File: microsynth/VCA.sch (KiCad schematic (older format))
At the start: 33 parts, among them J1 AudioJack3, J8 AudioJack2, Q9 BC548, U21 CA3080, U23 LM380N

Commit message: Replace dodgy parts 1458, 4136 & LF351s
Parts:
- U23: footprint Package_DIP:DIP-14_W7.62mm -> Package_DIP:DIP-14_W7.62mm_LongPads
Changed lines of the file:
@@
 F 0 "U23" H 7300 1700 50  0000 L CNN
 F 1 "LM380N" H 7400 1550 50  0000 L CNN
-F 2 "Package_DIP:DIP-14_W7.62mm" H 7350 1700 50  0001 C CIN
+F 2 "Package_DIP:DIP-14_W7.62mm_LongPads" H 7350 1700 50  0001 C CIN
 F 3 "http://www.ti.com/lit/ds/symlink/lm380.pdf" H 7350 1700 50  0001 C CNN
 	1    7350 1700

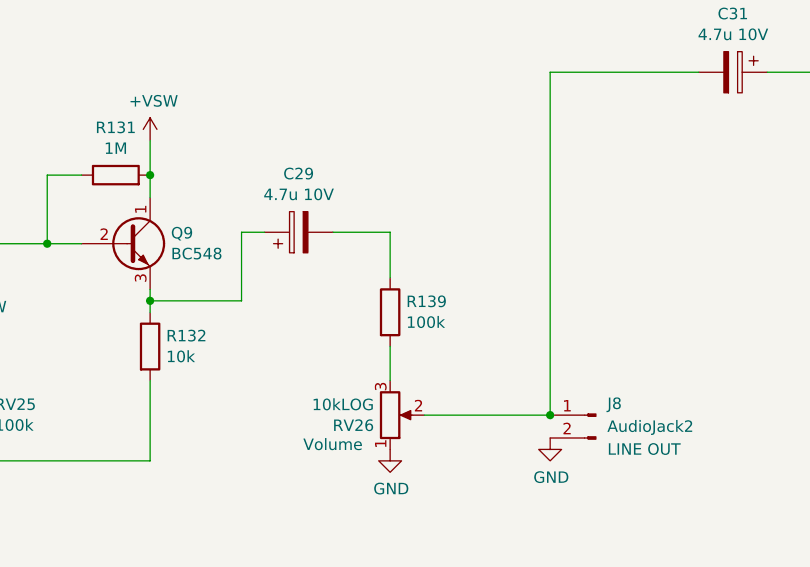
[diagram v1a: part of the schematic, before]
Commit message: Add test points
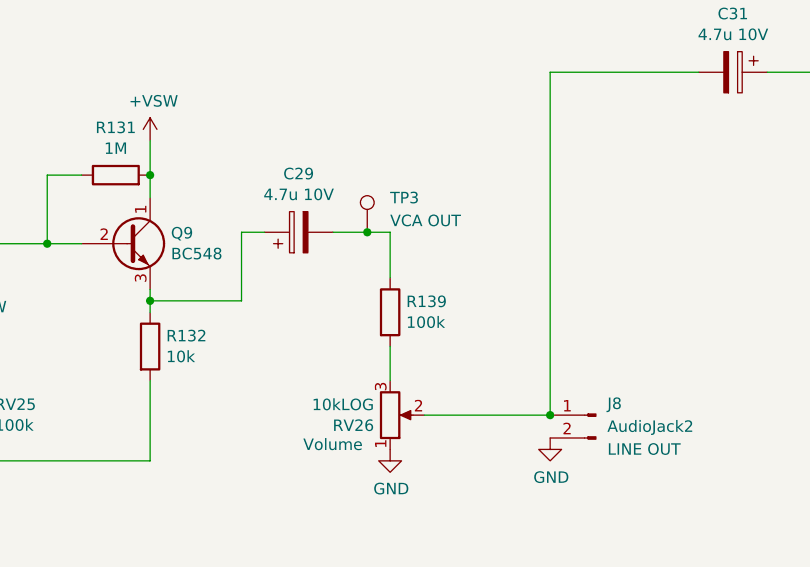
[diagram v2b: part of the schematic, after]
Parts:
- added TP3: VCA OUT, TestPoint:TestPoint_Pad_D2.0mm, symbol Connector:TestPoint
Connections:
- net at C29.2, R139.1: now also TP3.1
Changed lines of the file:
@@
 	3950 2800 3950 2750
 Wire Wire Line
-	4750 2500 5000 2500
+	4750 2500 4900 2500
 Wire Wire Line
 	5000 2500 5000 2700
@@
 	1    0    0    1
 $EndComp
-Wire Wire Line
-	5000 3150 5000 3000
 $Comp
 L power:GND #PWR?
@@
 $EndComp
 Connection ~ 5700 3300
+$Comp
+L Connector:TestPoint TP?
+U 1 1 5EE088D7
+P 4900 2500
+AR Path="/5E475532/5EE088D7" Ref="TP?"  Part="1"
+AR Path="/5E1B03E8/5EE088D7" Ref="TP3"  Part="1"
+F 0 "TP3" H 5000 2650 50  0000 L CNN
+F 1 "VCA OUT" H 5000 2550 50  0000 L CNN
+F 2 "TestPoint:TestPoint_Pad_D2.0mm" H 5100 2500 50  0001 C CNN
+F 3 "~" H 5100 2500 50  0001 C CNN
+	1    4900 2500
+	1    0    0    -1
+$EndComp
+Connection ~ 4900 2500
+Wire Wire Line
+	4900 2500 5000 2500
+Wire Wire Line
+	5000 3000 5000 3150
 $EndSCHEMATC

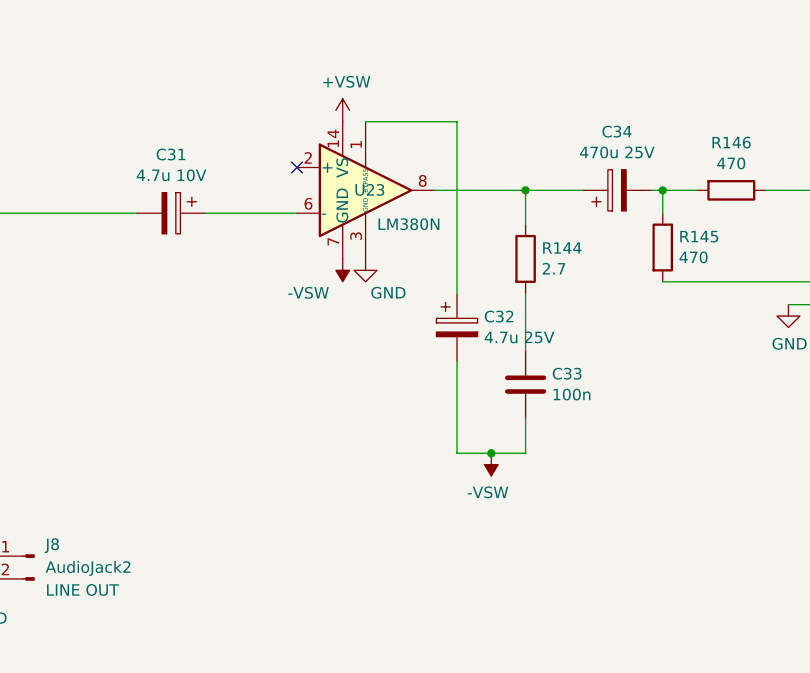
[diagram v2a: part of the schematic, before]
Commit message: Fix output amp
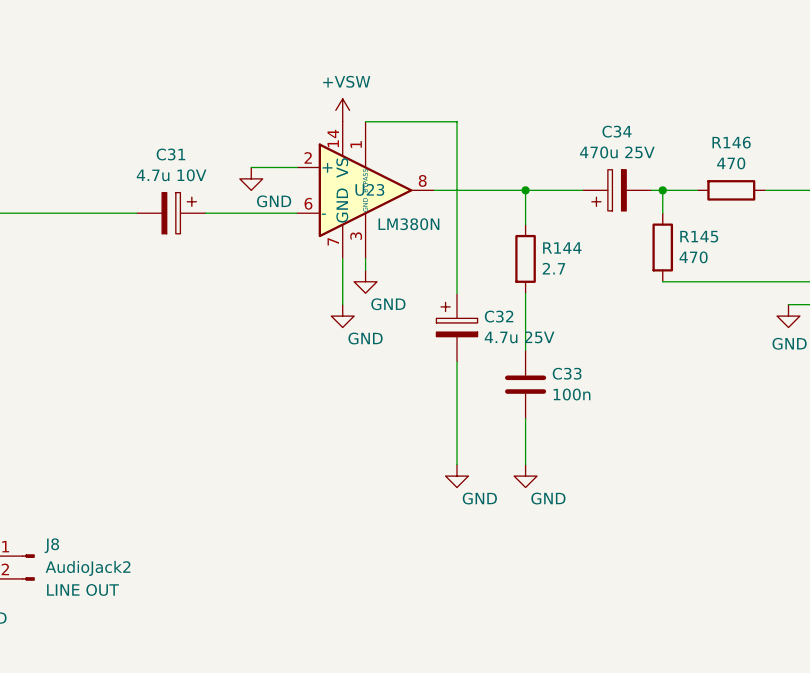
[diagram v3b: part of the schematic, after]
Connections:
- net -VSW: no longer C32.2, C33.2, U23.7 (GND)
- net GND: now also C32.2, C33.2, U23.2 (+), U23.7 (GND)
- no-connect marks 1 -> 0
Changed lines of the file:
@@
 	1    0    0    -1
-$EndComp
-$Comp
-L power:-VSW #PWR?
-U 1 1 5E1EC995
-P 7250 2000
-F 0 "#PWR?" H 7250 2100 50  0001 C CNN
-F 1 "-VSW" H 7400 2150 50  0000 C CNN
-F 2 "" H 7250 2000 50  0001 C CNN
-F 3 "" H 7250 2000 50  0001 C CNN
-	1    7250 2000
-	-1   0    0    1
 $EndComp
 Wire Wire Line
@@
 Wire Wire Line
 	8050 1700 8300 1700
-$Comp
-L power:-VSW #PWR?
-U 1 1 5E1F94DC
-P 7900 2850
-F 0 "#PWR?" H 7900 2950 50  0001 C CNN
-F 1 "-VSW" H 7915 3023 50  0000 C CNN
-F 2 "" H 7900 2850 50  0001 C CNN
-F 3 "" H 7900 2850 50  0001 C CNN
-	1    7900 2850
-	-1   0    0    1
-$EndComp
 Wire Wire Line
 	7050 1800 6650 1800
-NoConn ~ 7050 1600
 $Comp
 L Device:C C33
@@
 Wire Wire Line
 	8050 2400 8050 2150
-Wire Wire Line
-	8050 2700 8050 2850
-Wire Wire Line
-	8050 2850 7900 2850
-Wire Wire Line
-	7750 2450 7750 2850
-Connection ~ 7900 2850
-Wire Wire Line
-	7900 2850 7750 2850
 Text GLabel 1050 3450 0    50   BiDi ~ 0
 VCF_OUT
@@
 L power:GND #PWR?
 U 1 1 5EDD09AA
-P 7350 2000
-F 0 "#PWR?" H 7350 1750 50  0001 C CNN
-F 1 "GND" H 7450 1850 50  0000 C CNN
-F 2 "" H 7350 2000 50  0001 C CNN
-F 3 "" H 7350 2000 50  0001 C CNN
-	1    7350 2000
+P 7350 2050
+F 0 "#PWR?" H 7350 1800 50  0001 C CNN
+F 1 "GND" H 7450 1900 50  0000 C CNN
+F 2 "" H 7350 2050 50  0001 C CNN
+F 3 "" H 7350 2050 50  0001 C CNN
+	1    7350 2050
 	1    0    0    -1
 $EndComp
@@
 Wire Wire Line
 	5000 3000 5000 3150
+$Comp
+L power:GND #PWR?
+U 1 1 5F445670
+P 7250 2200
+F 0 "#PWR?" H 7250 1950 50  0001 C CNN
+F 1 "GND" H 7350 2050 50  0000 C CNN
+F 2 "" H 7250 2200 50  0001 C CNN
+F 3 "" H 7250 2200 50  0001 C CNN
+	1    7250 2200
+	1    0    0    -1
+$EndComp
+Wire Wire Line
+	7250 2000 7250 2200
+Wire Wire Line
+	7350 2050 7350 2000
+$Comp
+L power:GND #PWR?
+U 1 1 5F44B6B6
+P 6850 1600
+F 0 "#PWR?" H 6850 1350 50  0001 C CNN
+F 1 "GND" H 6950 1450 50  0000 C CNN
+F 2 "" H 6850 1600 50  0001 C CNN
+F 3 "" H 6850 1600 50  0001 C CNN
+	1    6850 1600
+	1    0    0    -1
+$EndComp
+Wire Wire Line
+	7050 1600 6850 1600
+$Comp
+L power:GND #PWR?
+U 1 1 5F44E816
+P 8050 2900
+F 0 "#PWR?" H 8050 2650 50  0001 C CNN
+F 1 "GND" H 8150 2750 50  0000 C CNN
+F 2 "" H 8050 2900 50  0001 C CNN
+F 3 "" H 8050 2900 50  0001 C CNN
+	1    8050 2900
+	1    0    0    -1
+$EndComp
+$Comp
+L power:GND #PWR?
+U 1 1 5F458F78
+P 7750 2900
+F 0 "#PWR?" H 7750 2650 50  0001 C CNN
+F 1 "GND" H 7850 2750 50  0000 C CNN
+F 2 "" H 7750 2900 50  0001 C CNN
+F 3 "" H 7750 2900 50  0001 C CNN
+	1    7750 2900
+	1    0    0    -1
+$EndComp
+Wire Wire Line
+	7750 2450 7750 2900
+Wire Wire Line
+	8050 2700 8050 2900
 $EndSCHEMATC

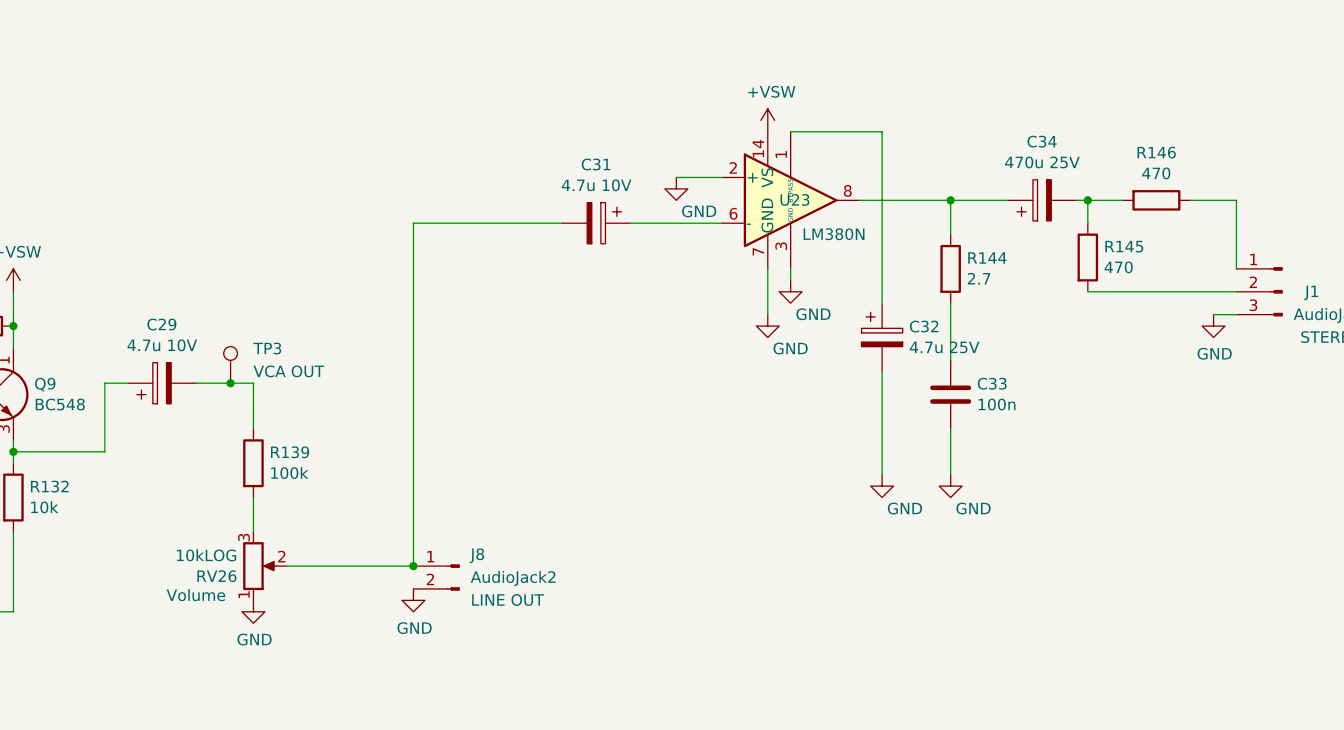
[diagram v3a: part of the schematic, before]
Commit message: Replace IC1 with LM348, update component values
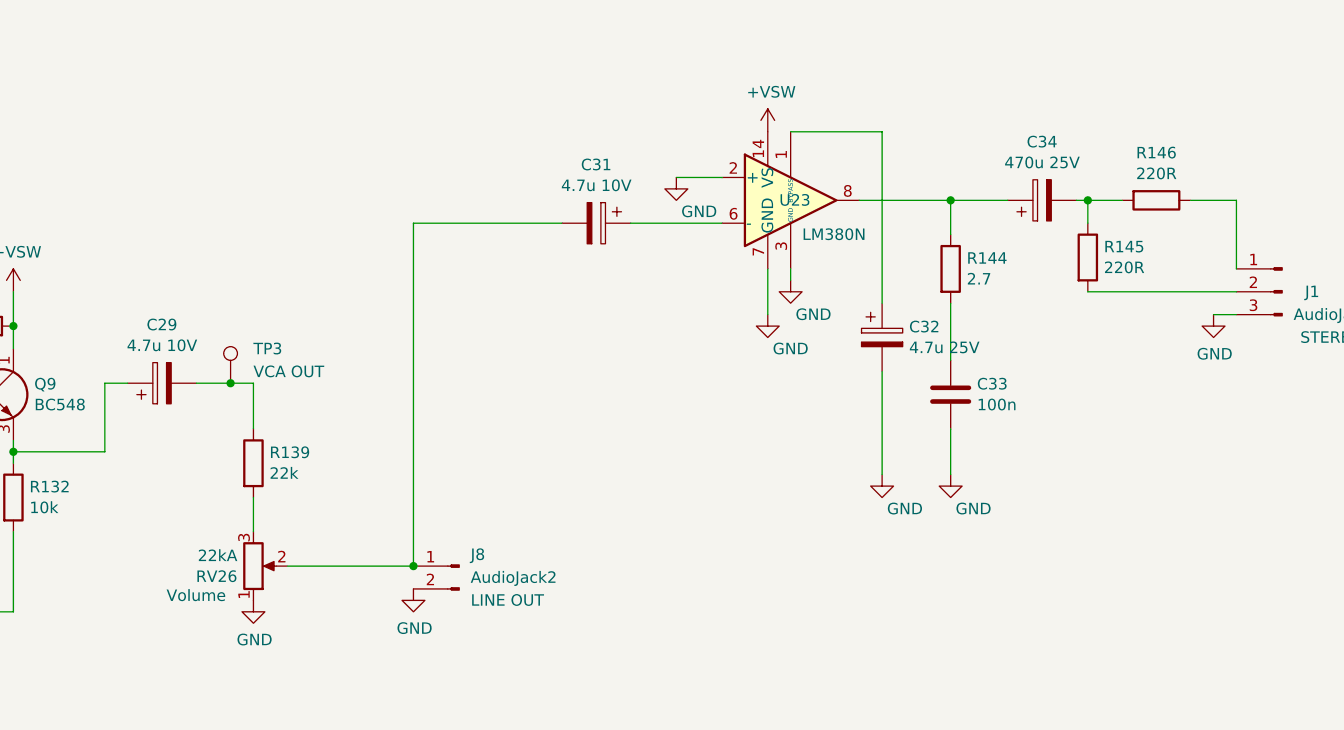
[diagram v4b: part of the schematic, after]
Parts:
- R139: value 100k -> 22k
- R145, R146: value 470 -> 220R
- RV26: value 10kLOG -> 22kA
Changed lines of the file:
@@
 P 5000 2850
 F 0 "R139" H 5070 2896 50  0000 L CNN
-F 1 "100k" H 5070 2805 50  0000 L CNN
+F 1 "22k" H 5070 2805 50  0000 L CNN
 F 2 "Resistor_THT:R_Axial_DIN0207_L6.3mm_D2.5mm_P10.16mm_Horizontal" V 4930 2850 50  0001 C CNN
 F 3 "~" H 5000 2850 50  0001 C CNN
@@
 P 5000 3300
 F 0 "RV26" H 4930 3346 50  0000 R CNN
-F 1 "10kLOG" H 4930 3255 50  0000 R CNN
+F 1 "22kA" H 4930 3255 50  0000 R CNN
 F 2 "Connector_PinHeader_2.54mm:PinHeader_1x03_P2.54mm_Vertical" H 5000 3300 50  0001 C CNN
 F 3 "~" H 5000 3300 50  0001 C CNN
@@
 P 8950 1700
 F 0 "R146" V 8743 1700 50  0000 C CNN
-F 1 "470" V 8834 1700 50  0000 C CNN
+F 1 "220R" V 8834 1700 50  0000 C CNN
 F 2 "Resistor_THT:R_Axial_DIN0207_L6.3mm_D2.5mm_P10.16mm_Horizontal" V 8880 1700 50  0001 C CNN
 F 3 "~" H 8950 1700 50  0001 C CNN
@@
 P 8650 1950
 F 0 "R145" H 8720 1996 50  0000 L CNN
-F 1 "470" H 8720 1905 50  0000 L CNN
+F 1 "220R" H 8720 1905 50  0000 L CNN
 F 2 "Resistor_THT:R_Axial_DIN0207_L6.3mm_D2.5mm_P10.16mm_Horizontal" V 8580 1950 50  0001 C CNN
 F 3 "~" H 8650 1950 50  0001 C CNN
